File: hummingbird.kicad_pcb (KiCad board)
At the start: 2 copper layers, 43 parts, among them J1 JST, J2 ANEMOMETER, J3 USB_B_Micro, J4 Expansion, J5 SWD_PROG, J6 microSD, J7 SOIC_CLIP, J8 Antenna, J9 Conn_Coaxial, SW1 SW_DPDT_x2, U1 MCP73831-2-OT, U2 AP2112K-3.3, U3 W25Q64JVSSIM, U4 ATSAMD21G18A-AUT, U5 RFM95W-915S2, U6 BMP388, Y1 32.768 Hz

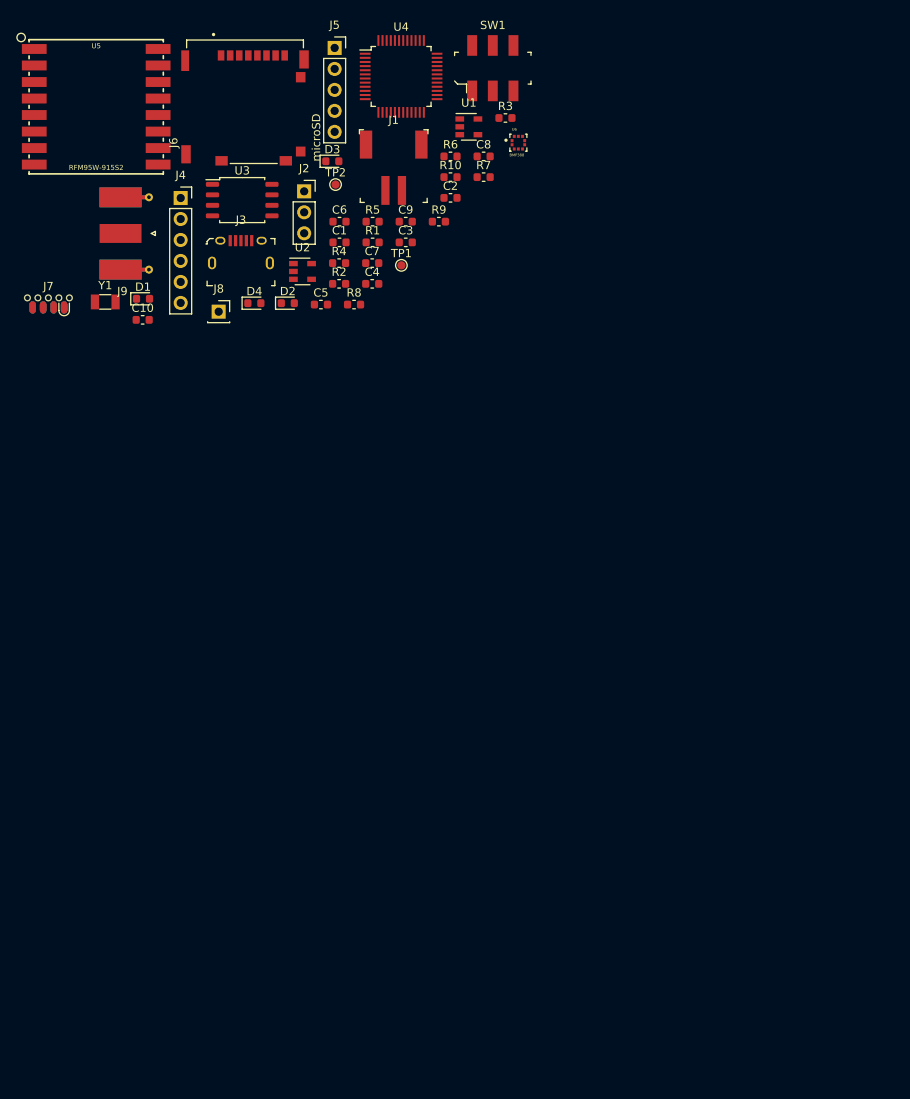
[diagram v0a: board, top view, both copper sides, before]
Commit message: remove SMA and some routing
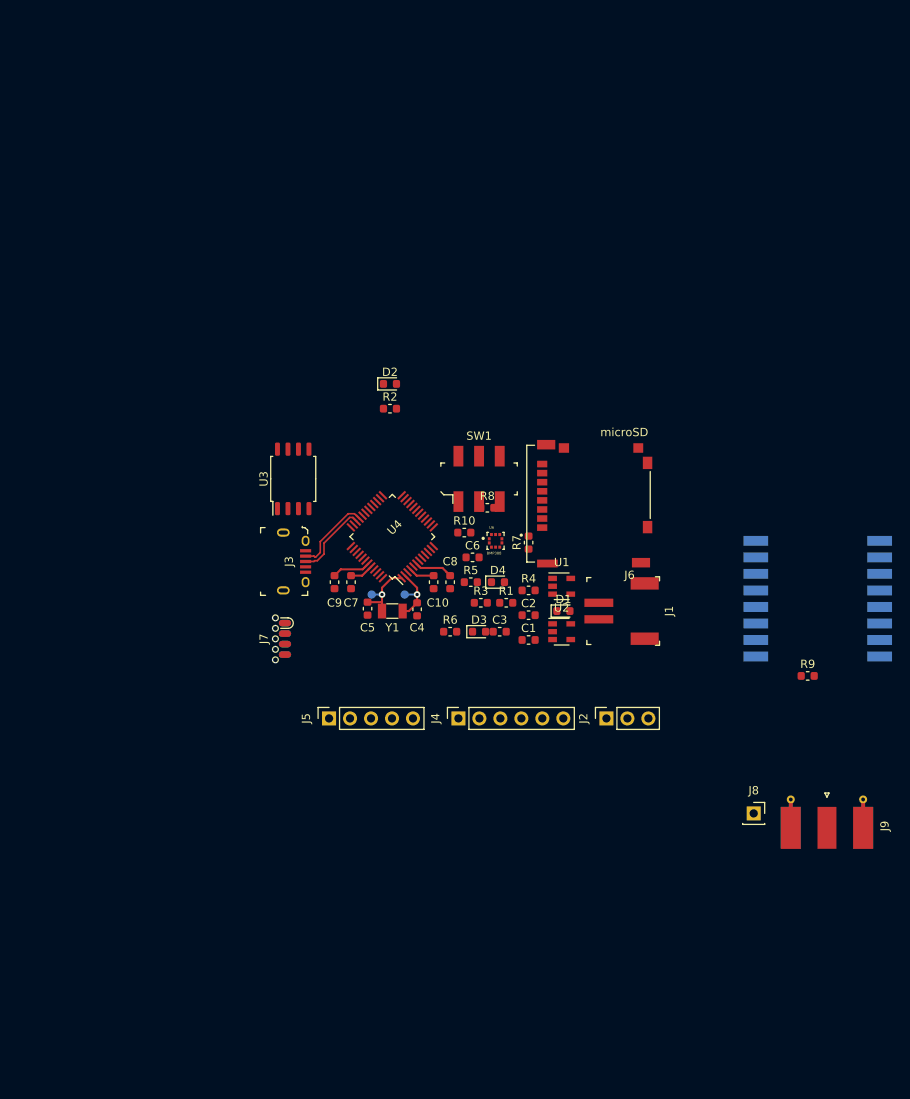
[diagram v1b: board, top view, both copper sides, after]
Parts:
- TP1, TP2, U5: moved to B.Cu
- moved J9 109.4 mm to (169.1, 146.0), turned to 90 degrees
- moved U5 105.7 mm to (168.0, 120.0)
- moved J8 88.8 mm to (160.2, 146.0)
- moved J5 81.2 mm to (108.8, 134.5), turned to 90 degrees
- moved J2 73.6 mm to (142.4, 134.5), turned to 90 degrees
- moved J4 71.4 mm to (124.5, 134.5), turned to 90 degrees
- moved R9 70.8 mm to (166.8, 129.4)
- moved J6 63.9 mm to (141.0, 108.5), turned to 90 degrees
- moved D1 63.4 mm to (137.2, 121.5)
- moved D3 59.7 mm to (127.0, 124.0)
- moved R3 58.8 mm to (127.2, 120.5)
- moved R6 57.5 mm to (123.5, 124.0)
- moved U1 56.7 mm to (137.0, 118.5)
- moved J1 56.7 mm to (141.5, 121.5), turned to 270 degrees
- moved U4 55.7 mm to (116.5, 112.5), turned to 135 degrees
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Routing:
- net /USB_D-: track 0.00 -> 9.76 mm
- net /USB_D+: track 0.00 -> 9.39 mm
- net Net-(C5-Pad2): track 0.00 -> 8.72 mm, vias 0 -> 1
- net Net-(C4-Pad2): track 0.00 -> 7.62 mm, vias 0 -> 1
- net +3V3: track 0.00 -> 7.62 mm
- net Net-(C9-Pad2): track 0.00 -> 4.71 mm
- net /AREF: track 0.00 -> 3.12 mm

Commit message: rough placement (gonna try the autorouter)
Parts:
- removed J9: Conn_Coaxial, footprints:SMA_Molex_73251-1153_EdgeMount_Horizontal
- R9: moved to B.Cu
- moved U5 57.0 mm to (112.0, 109.5)
- moved J8 56.6 mm to (124.0, 102.5)
- moved R9 46.6 mm to (124.0, 110.8), turned to 90 degrees
- moved SW1 29.4 mm to (105.5, 125.5), turned to 180 degrees
- moved D3 25.4 mm to (113.0, 102.8), turned to 90 degrees
- moved U2 24.6 mm to (112.5, 126.0), turned to 180 degrees
- moved R6 22.9 mm to (115.0, 102.8), turned to 90 degrees
- moved R8 19.0 mm to (109.0, 107.7), turned to 90 degrees
- moved C1 17.0 mm to (116.0, 125.8), turned to 90 degrees
- moved D1 15.8 mm to (122.0, 125.8), turned to 270 degrees
- moved R4 14.6 mm to (120.0, 125.7), turned to 270 degrees
- moved U6 13.8 mm to (120.0, 102.5), turned to 180 degrees
- moved U1 13.7 mm to (125.5, 126.0), turned to 180 degrees
- moved R10 12.3 mm to (117.0, 102.8), turned to 90 degrees
- moved R7 12.3 mm to (123.0, 106.0)
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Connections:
- net /ANTENNA renamed Net-(J8-Pad1)
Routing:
- net +3V3: track 7.62 -> 10.9 mm

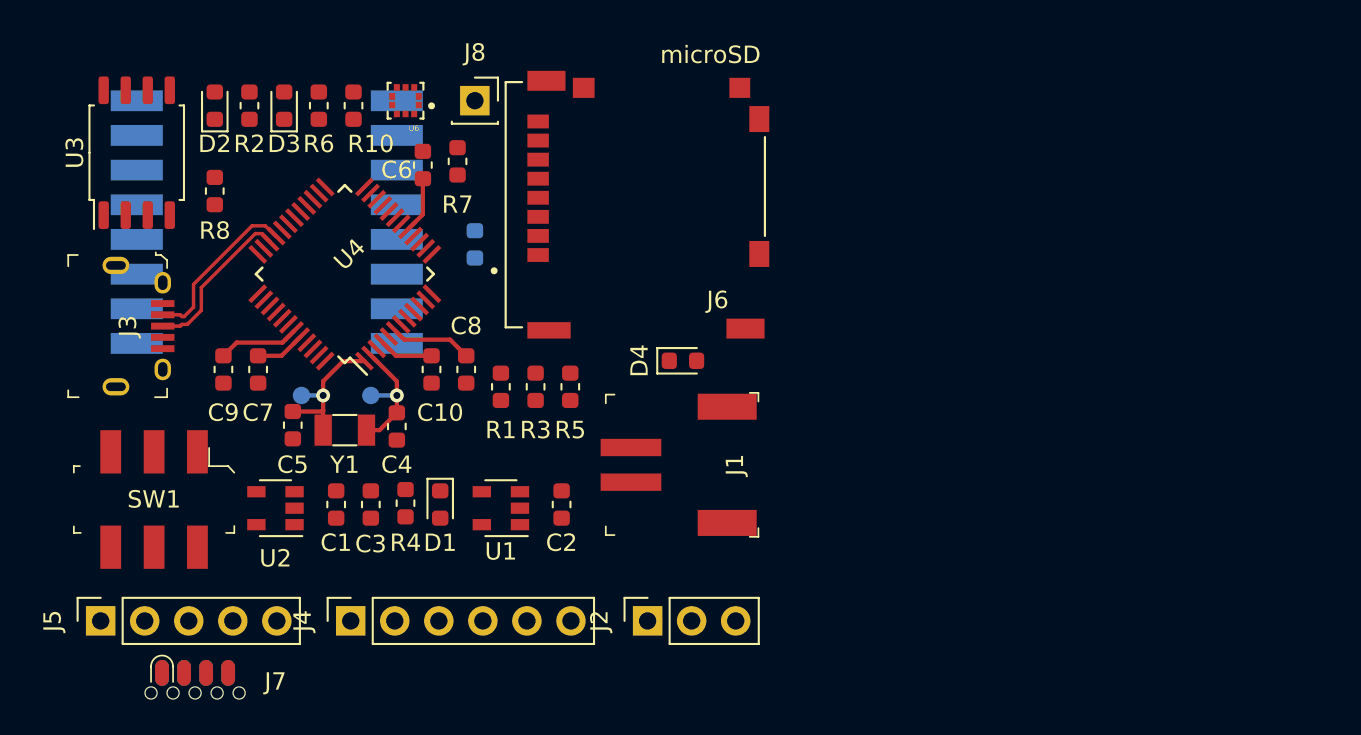
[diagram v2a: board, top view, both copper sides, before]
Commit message: remove SOICbyte, start layout over, rejigger pinouts
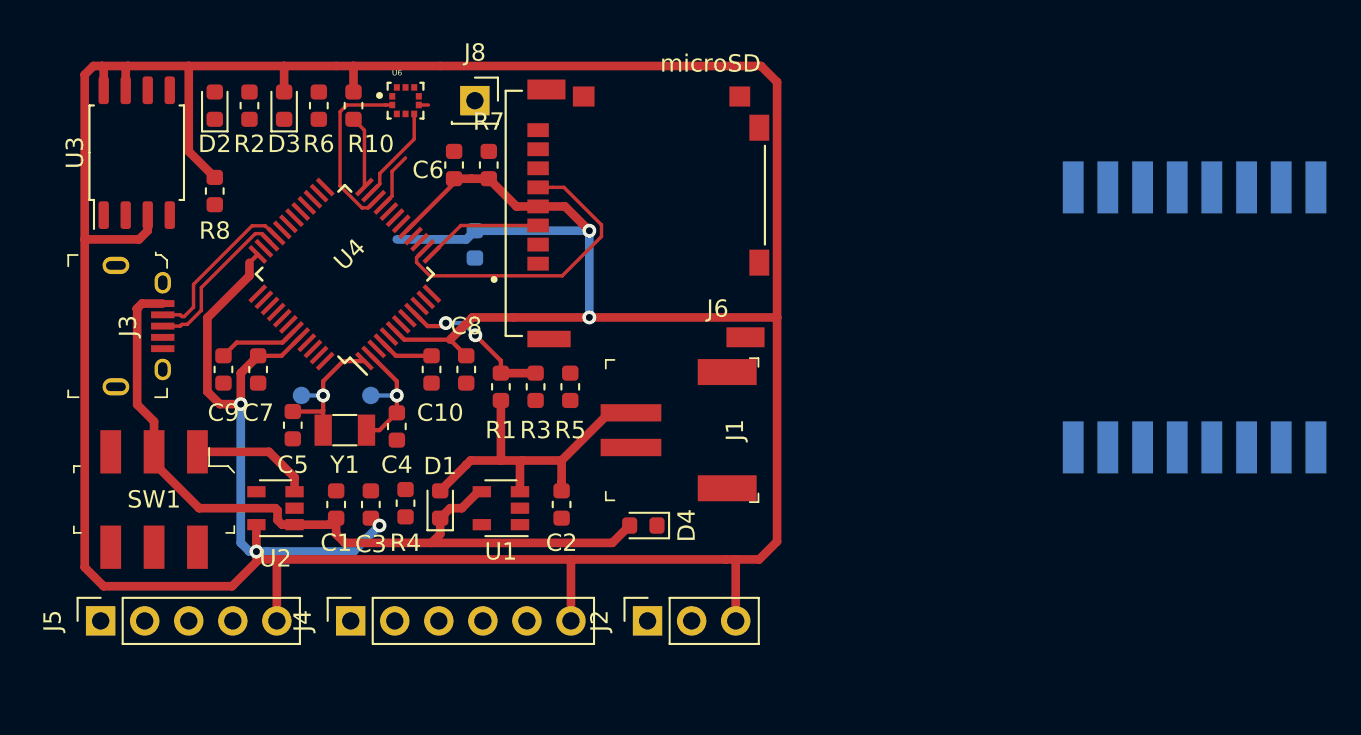
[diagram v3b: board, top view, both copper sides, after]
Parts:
- removed J7: SOIC_CLIP, footprints:SOIC_clipProgSmall
- moved U5 53.8 mm to (165.5, 115.0), turned to 90 degrees
- moved D4 9.77 mm to (133.7, 127.0), turned to 180 degrees
- moved J1 2.00 mm to (133.0, 121.5)
- moved R7 1.81 mm to (124.8, 106.2), turned to 270 degrees
- moved C6 1.80 mm to (122.8, 106.2)
- moved J6 0.50 mm to (134.0, 109.0)
- turned D1 to 90 degrees
- turned U6 to 0 degrees
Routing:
- net +3V3: track 10.9 -> 255.8 mm, vias 0 -> 5
- net VBUS: track 0.00 -> 46.5 mm
- net +BATT: track 0.00 -> 19.9 mm
- net /microSD_SCK: track 0.00 -> 18.2 mm
- net /BMP388_SCK: track 0.00 -> 10.3 mm
- net /BATT_V: track 0.00 -> 9.06 mm, vias 0 -> 2
- net Net-(SW1-Pad1): track 0.00 -> 7.04 mm
- net /microSD_MOSI: track 0.00 -> 6.82 mm
- net /BMP388_MISO: track 0.00 -> 5.61 mm
- net /BMP388_CS: track 0.00 -> 4.72 mm
- net /BMP388_MOSI: track 0.00 -> 3.28 mm
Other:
- rule trace_min: 0.2 -> 0.01
- rule via_min_drill: 0.3 -> 0.254
- rule via_min_size: 0.4 -> 0.508

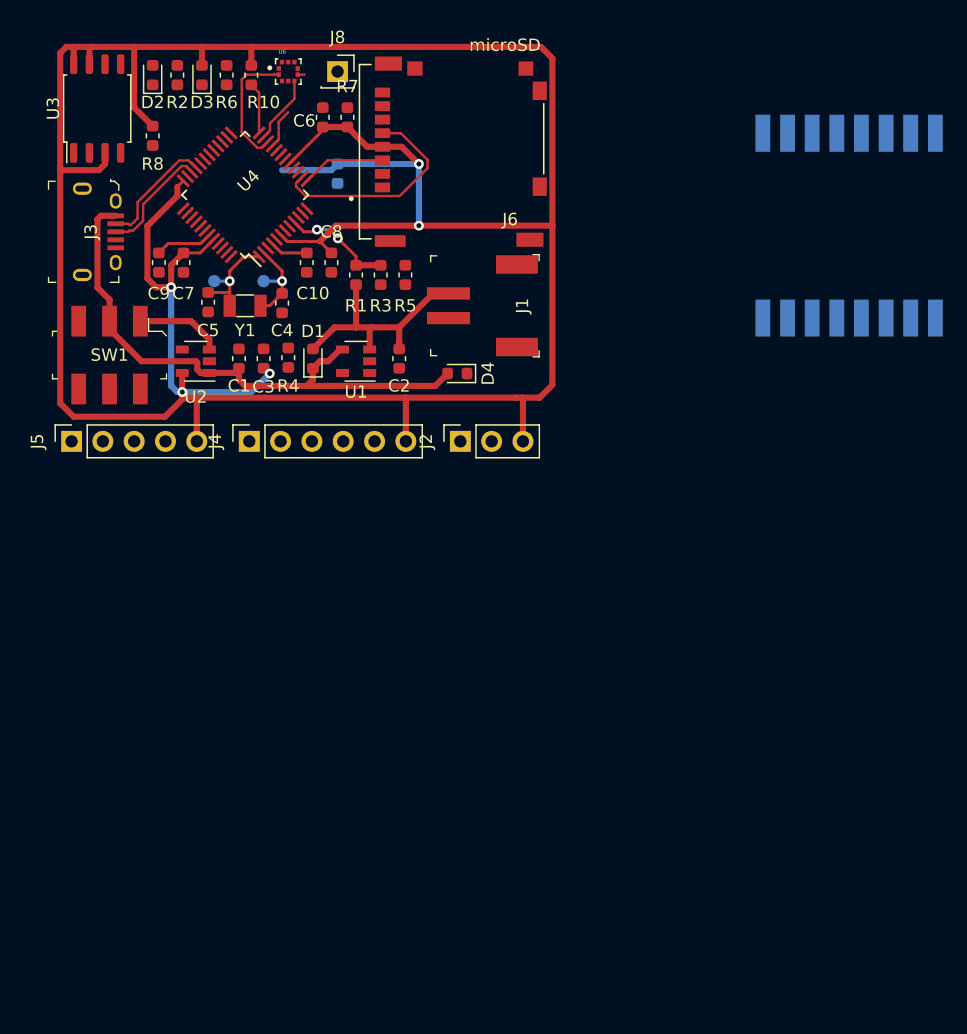
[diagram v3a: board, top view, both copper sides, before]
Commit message: move PCB to right file name
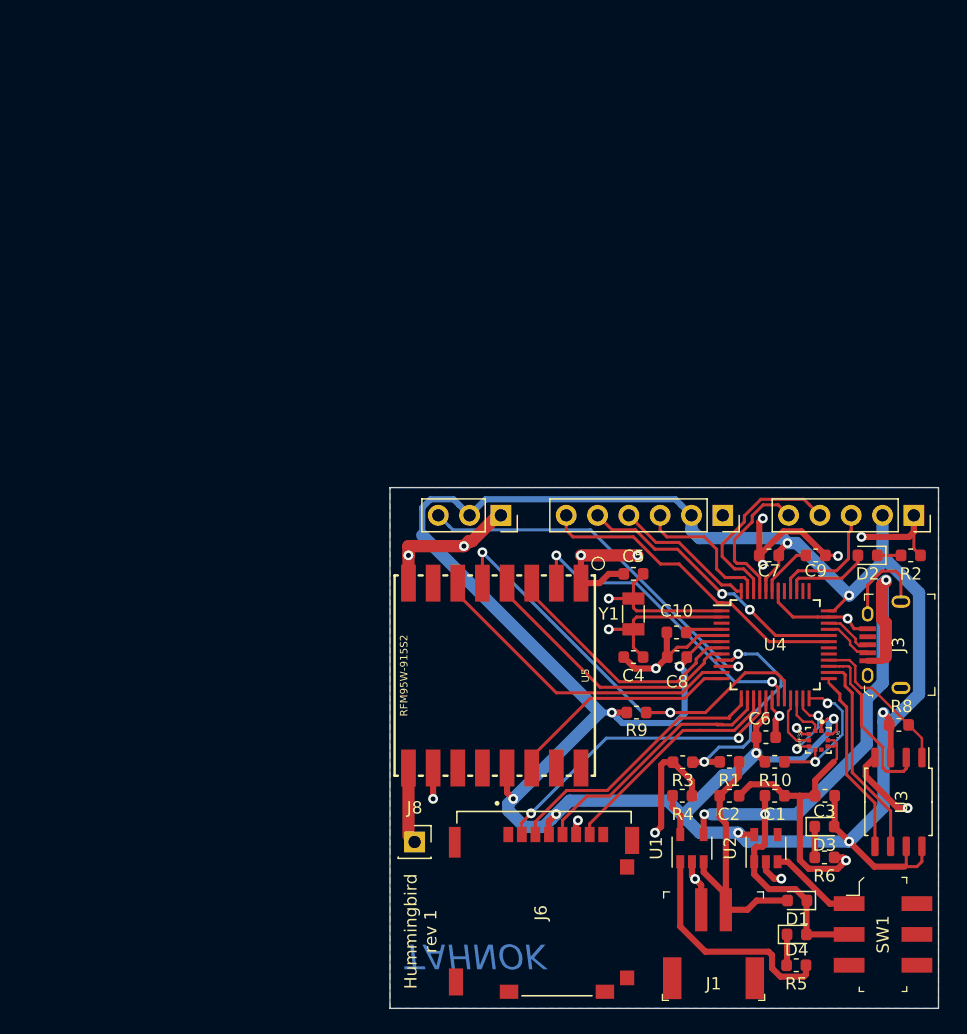
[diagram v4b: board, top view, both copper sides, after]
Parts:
- removed R7: 10k, footprints:R_0603_1608Metric
- added REF**: hummingbird, footprints:hummingbird, B.Cu at (154.0, 173.8)
- R9, U5: moved to F.Cu
- moved U3 86.0 mm to (169.5, 161.8), turned to 270 degrees
- moved R6 79.9 mm to (163.5, 166.2), turned to 0 degrees
- moved D3 79.2 mm to (163.5, 163.8), turned to 0 degrees
- moved SW1 78.4 mm to (168.2, 172.5), turned to 270 degrees
- moved R8 77.1 mm to (169.5, 155.5), turned to 180 degrees
- moved R2 71.1 mm to (170.5, 141.8), turned to 0 degrees
- moved R10 70.0 mm to (159.5, 158.5), turned to 180 degrees
- moved D2 69.9 mm to (167.0, 141.8), turned to 180 degrees
- moved J3 69.6 mm to (167.0, 149.0), turned to 90 degrees
- moved U6 69.2 mm to (163.0, 156.8), turned to 270 degrees
- moved J5 68.6 mm to (170.8, 138.5), turned to 270 degrees
- moved R5 64.4 mm to (161.2, 175.0), turned to 0 degrees
- moved J8 62.8 mm to (130.2, 165.0)
- moved J6 62.1 mm to (140.8, 170.8), turned to 0 degrees
- moved C6 61.8 mm to (158.8, 156.5), turned to 180 degrees
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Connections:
- J2 pad 2: /ANEN_INT -> +3V3
- J2 pad 3: +3V3 -> /ANEN_INT
- J4 pad 2: /SERIAL_TX -> +3V3
- J4 pad 3: /SERIAL_RX -> /SERIAL_TX
- J4 pad 4: /I2C_SCL -> /SERIAL_RX
- J4 pad 5: /I2C_SDA -> /I2C_SCL
- J4 pad 6: +3V3 -> /I2C_SDA
- J5 pad 2: /RESET -> +3V3
- J5 pad 3: /SWDIO -> /RESET
- J5 pad 4: /SWCLK -> /SWDIO
- J5 pad 5: +3V3 -> /SWCLK
- U4 pad 11: Net-(U4-Pad11) -> /LORA_RESET
- U4 pad 12: Net-(U4-Pad12) -> /LORA_INT
- U4 pad 37: /LORA_RESET -> Net-(U4-Pad37)
- U4 pad 38: /LORA_INT -> Net-(U4-Pad38)
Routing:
- net GND: track 0.00 -> 129.0 mm, vias 0 -> 19
- net +3V3: track 255.8 -> 212.8 mm, vias 5 -> 11
- net /LORA_CS: track 0.00 -> 38.3 mm, vias 0 -> 2
- net /ANEN_INT: track 0.00 -> 30.8 mm, vias 0 -> 1
- net /I2C_SDA: track 0.00 -> 26.7 mm
- net /LORA_RESET: track 0.00 -> 26.3 mm
- net /LORA_MISO: track 0.00 -> 25.6 mm, vias 0 -> 2
- net /microSD_CS: track 0.00 -> 25.3 mm, vias 0 -> 2
- net /I2C_SCL: track 0.00 -> 22.8 mm, vias 0 -> 2
- net /LORA_SCK: track 0.00 -> 22.7 mm
- net /LORA_MOSI: track 0.00 -> 20.6 mm
- net /microSD_MISO: track 0.00 -> 19.2 mm
- net /LORA_INT: track 0.00 -> 18.9 mm
- net Net-(R5-Pad2): track 0.00 -> 18.6 mm
- net /FLASH_SCK: track 0.00 -> 16.9 mm
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- added copper zone on B.Cu, net GND
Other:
- board outline added: 44.5 x 42.2 mm
- board text added: "3V3"
- board text added: "ANEM"
- board text added: "ANT"
- board text added: "GND"
- board text added: "Hummingbird rev 1"
- board text added: "I2C SCL"
- board text added: "I2C SDA"
- board text added: "RESET"
- board text added: "RX"
- board text added: "SWCLK"
- board text added: "SWDIO"
- board text added: "TAHNOK"
- board text added: "TX"

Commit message: add gerbers for r1 production run!
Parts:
- moved REF** 3.82 mm to (157.2, 175.8)
